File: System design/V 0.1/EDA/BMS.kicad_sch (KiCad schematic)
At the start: 20 parts, among them J1 Conn_01x03_Pin, J2 Conn_01x02_Pin, Q1 NMOS, Q2 NMOS, Q3 PMOS, Q4 PMOS, U1 SN74LVC2G14DBV, U2 SN74LVC2G14DBV, U3 CDSOT236-0504C

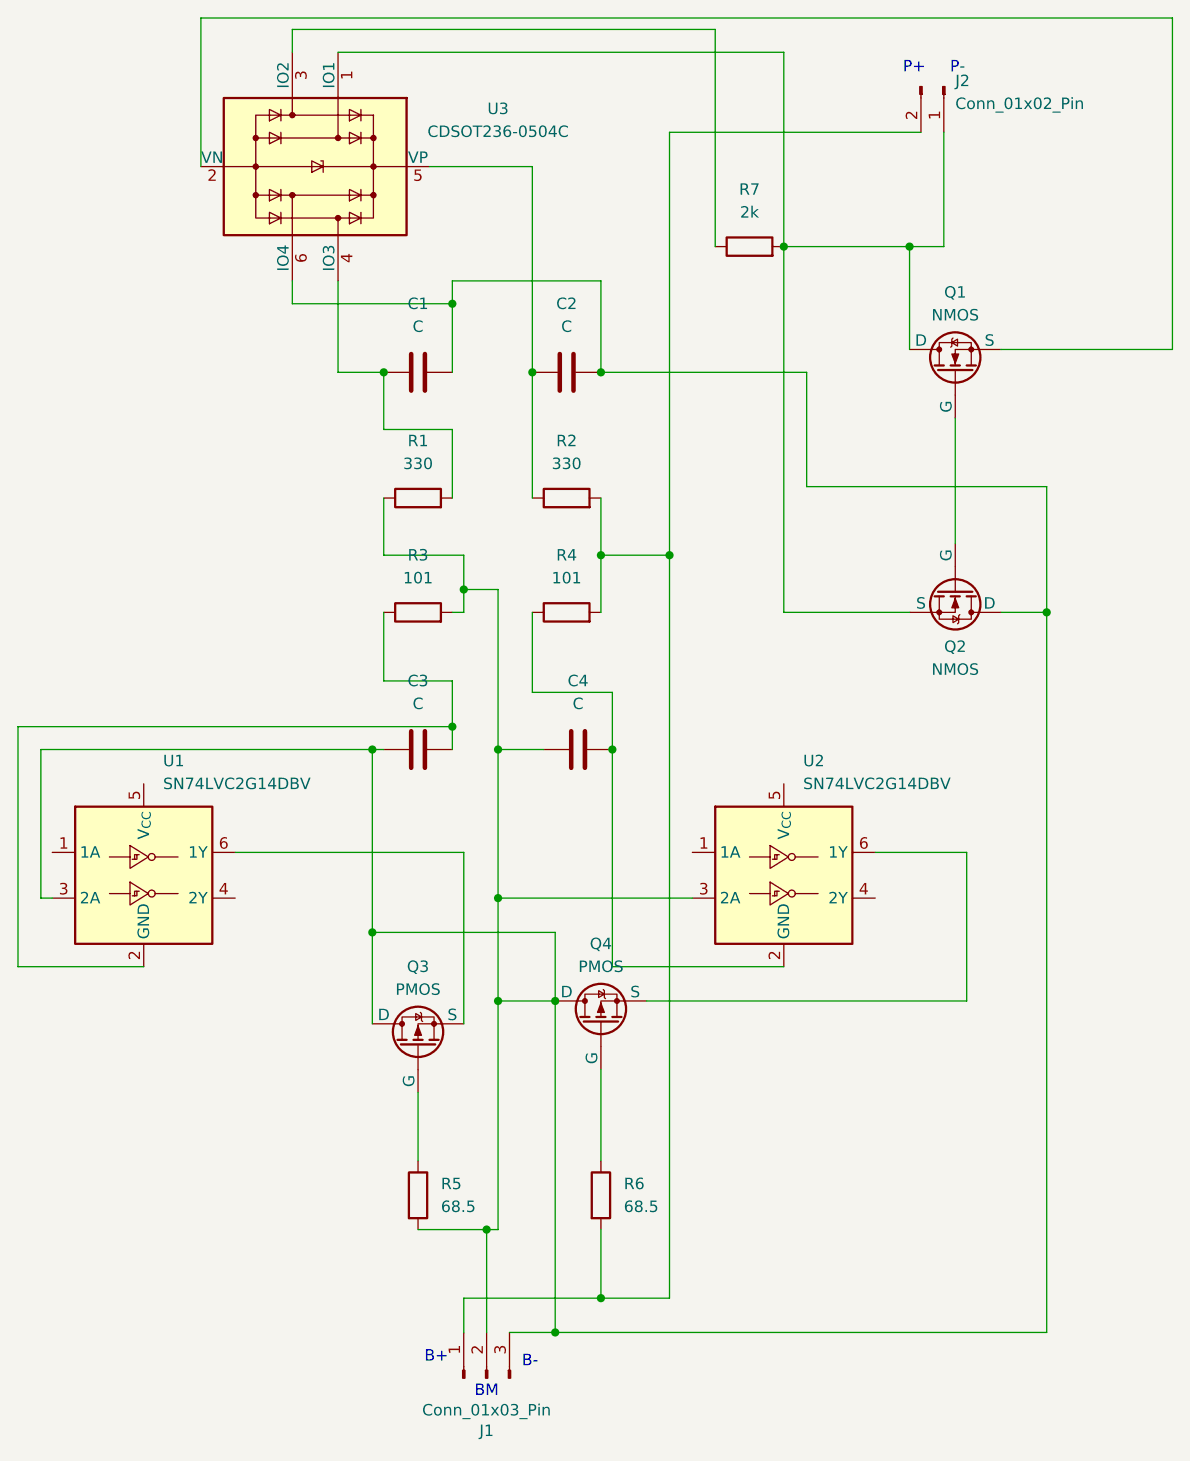
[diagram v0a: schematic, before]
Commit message: Updated PCB (BMS)
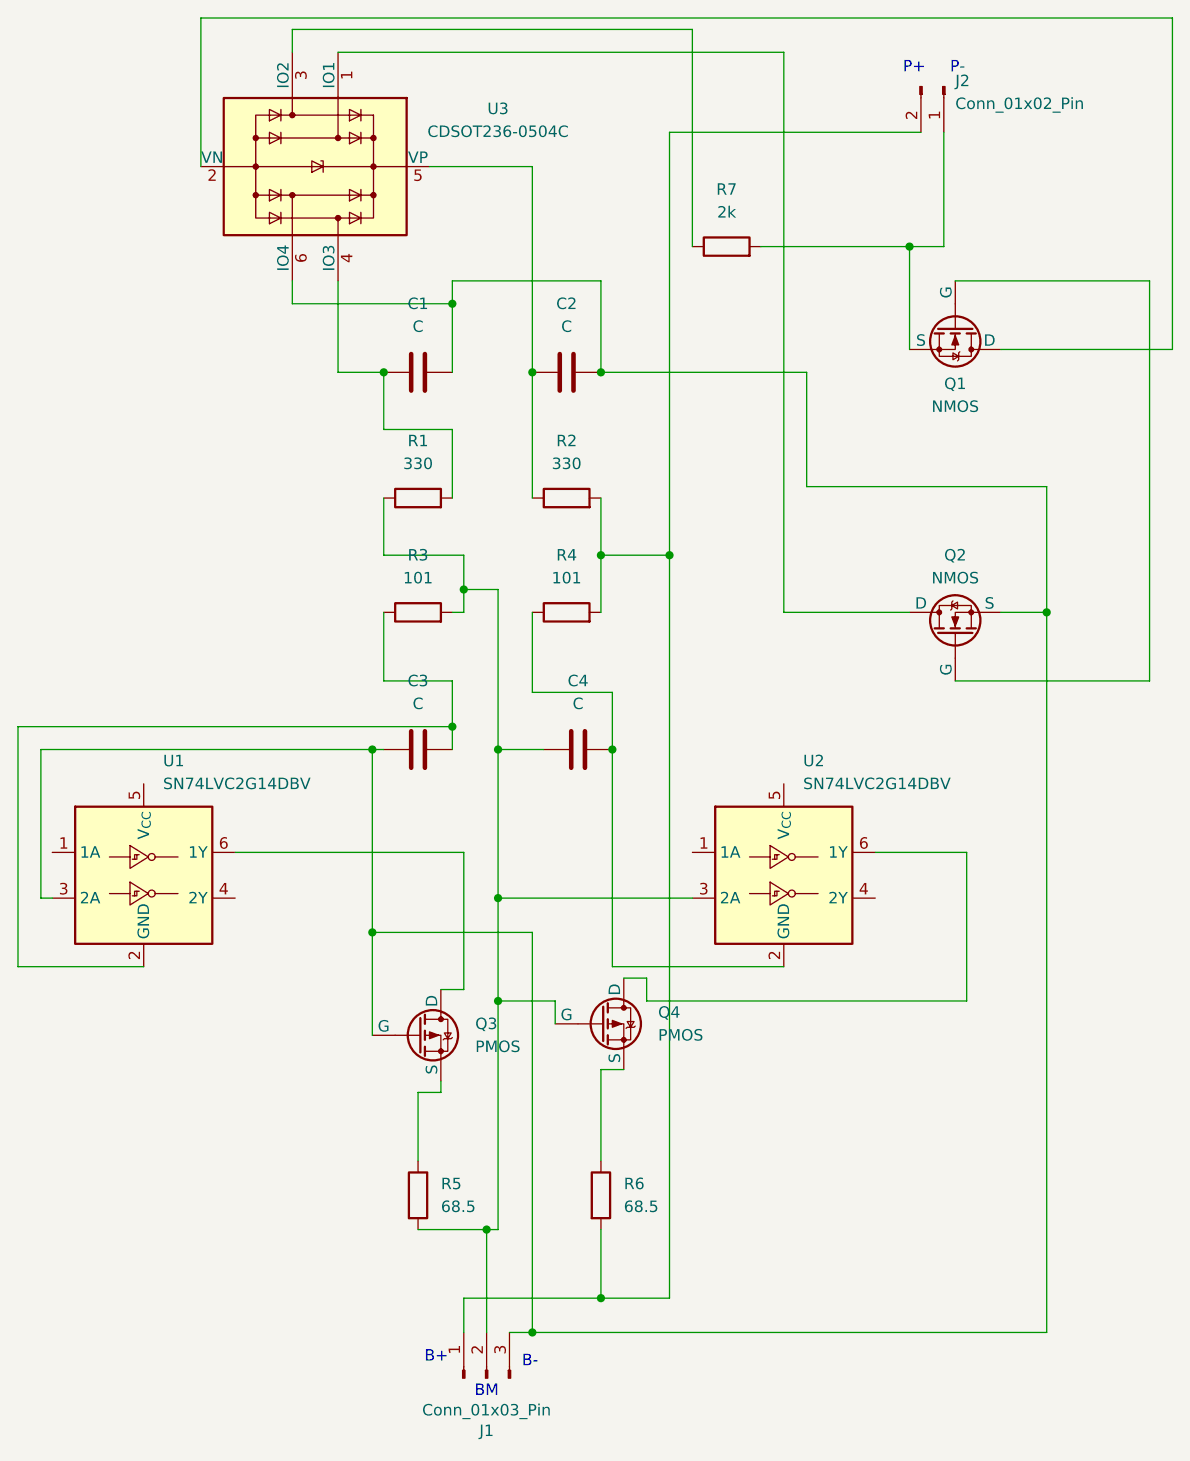
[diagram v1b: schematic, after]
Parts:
- C1, C2, C3, C4: footprint Capacitor_SMD:C_1206_3216Metric_Pad1.33x1.80mm_HandSolder -> Capacitor_SMD:C_0603_1608Metric_Pad1.08x0.95mm_HandSolder
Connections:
- net at U2.6 (1Y): now also Q4.1 (D); no longer Q4.3 (S)
- net at Q4.2 (G): now also C4.1, J1.2 (Pin_2), R1.1, R3.2, R5.2, U2.3 (2A); no longer R6.1
- net at Q3.2 (G): now also C1.2, C2.2, C3.1, J1.3 (Pin_3), Q2.3 (S), U1.3 (2A), U3.6 (IO4); no longer R5.1
- net at U1.6 (1Y): now also Q3.1 (D); no longer Q3.3 (S)
- net at Q1.3 (S): now also J2.1 (Pin_1), R7.2; no longer U3.2 (VN)
- new net: Q4.3 (S), R6.1
- new net: Q3.3 (S), R5.1
- new net: Q2.1 (D), U3.1 (IO1)
- new net: Q1.1 (D), U3.2 (VN)
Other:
- moved on the sheet: Q1, Q2, Q3, Q4, R7

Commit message: PCB modified
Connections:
- net GND: now reaches J2.1 (Pin_1), Q1.3 (S), R7.2
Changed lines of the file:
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@@
+	)
+	(junction
+		(at 116.84 31.75)
+		(diameter 0)
+		(color 0 0 0 0)
 	)
 	(junction
@@
 	(wire
 		(pts
+			(xy 116.84 31.75) (xy 116.84 39.37)
+		)
+		(stroke
+			(width 0)
+			(type default)
+		)
+	)
+	(wire
+		(pts
 			(xy 71.12 88.9) (xy 80.01 88.9)
 		)
@@
 	(wire
 		(pts
+			(xy 116.84 31.75) (xy 121.92 31.75)
+		)
+		(stroke
+			(width 0)
+			(type default)
+		)
+	)
+	(wire
+		(pts
 			(xy 101.6 66.04) (xy 128.27 66.04)
 		)
@@
 	(wire
 		(pts
-			(xy 116.84 26.67) (xy 116.84 39.37)
+			(xy 116.84 26.67) (xy 116.84 31.75)
 		)
 		(stroke
@@
 					(unit 1)
 				)
+			)
+		)
+	)
+	(symbol
+		(lib_id "power:GND")
+		(at 121.92 31.75 0)
+		(unit 1)
+		(exclude_from_sim no)
+		(in_bom yes)
+		(on_board yes)
+		(dnp no)
+		(fields_autoplaced yes)
+		(property "Reference" "#PWR01"
+			(at 121.92 38.1 0)
+			(effects
+				(font
+					(size 1.27 1.27)
+				)
+				(hide yes)
+			)
+		)
+		(property "Value" "GND"
+			(at 121.92 36.83 0)
+			(effects
+				(font
+					(size 1.27 1.27)
+				)
+			)
+		)
+		(property "Footprint" ""
+			(at 121.92 31.75 0)
+			(effects
+				(font
+					(size 1.27 1.27)
+				)
+				(hide yes)
+			)
+		)
+		(property "Datasheet" ""
+			(at 121.92 31.75 0)
+			(effects
+				(font
+					(size 1.27 1.27)
+				)
+				(hide yes)
+			)
+		)
+		(property "Description" "Power symbol creates a global label with name \"GND\" , ground"
+			(at 121.92 31.75 0)
+			(effects
+				(font
+					(size 1.27 1.27)
+				)
+				(hide yes)
+			)
+		)
+		(pin "1"
+		)
+		(instances
+			(project ""
+				(path "/fa29bee4-ac79-474e-bb50-2540228b9014"
+					(reference "#PWR01")
+					(unit 1)
+				)
